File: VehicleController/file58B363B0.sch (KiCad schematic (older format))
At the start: 5 parts, among them P4 CONN_01X02, P5 MX150_8, U9 MCP2551

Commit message: Begin nailing down VC schematic details
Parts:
- added D10, D9: LED_Yel, symbol LED_Small_ALT
- added R19, R20: R_Small, symbol R_Small
- added U11: NDC7002N, symbol NDC7002N
- renumbered C11 to C12, P4 to P3, P5 to P4, R11 to R18, U9 to U12
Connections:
- net +5V: now also R19.1, R20.1
- net CANRX: now also U11.3 (G2)
- net CANTX: now also U11.1 (G1)
- net GND: now also U11.2 (S2), U11.5 (S1)
- new net: D10.1 (K), U11.4 (D2)
- new net: D9.1 (K), U11.6 (D1)
- new net: D9.2 (A), R19.2
- new net: D10.2 (A), R20.2
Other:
- moved on the sheet: C12
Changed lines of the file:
@@
 $EndDescr
 $Comp
-L MCP2551 U9
+L MCP2551 U12
 U 1 1 58B36586
 P 5450 3250
-F 0 "U9" H 5450 3737 60  0000 C CNN
+F 0 "U12" H 5450 3737 60  0000 C CNN
 F 1 "MCP2551" H 5450 3631 60  0000 C CNN
 F 2 "" H 5450 3250 60  0000 C CNN
@@
 $EndComp
 $Comp
-L GND #PWR040
+L GND #PWR46
 U 1 1 58B3658D
 P 5950 3500
-F 0 "#PWR040" H 5950 3250 50  0001 C CNN
+F 0 "#PWR46" H 5950 3250 50  0001 C CNN
 F 1 "GND" H 5955 3327 50  0000 C CNN
 F 2 "" H 5950 3500 50  0000 C CNN
@@
 NoConn ~ 5850 3050
 $Comp
-L +5V #PWR041
+L +5V #PWR44
 U 1 1 58B36594
 P 4900 2950
-F 0 "#PWR041" H 4900 2800 50  0001 C CNN
+F 0 "#PWR44" H 4900 2800 50  0001 C CNN
 F 1 "+5V" H 4915 3123 50  0000 C CNN
 F 2 "" H 4900 2950 50  0000 C CNN
@@
 $EndComp
 $Comp
-L GND #PWR042
+L GND #PWR45
 U 1 1 58B3659A
 P 4950 3550
-F 0 "#PWR042" H 4950 3300 50  0001 C CNN
+F 0 "#PWR45" H 4950 3300 50  0001 C CNN
 F 1 "GND" H 4955 3377 50  0000 C CNN
 F 2 "" H 4950 3550 50  0000 C CNN
@@
 $EndComp
 $Comp
-L R R11
+L R R18
 U 1 1 58B365A2
 P 5250 2500
-F 0 "R11" V 5043 2500 50  0000 C CNN
+F 0 "R18" V 5043 2500 50  0000 C CNN
 F 1 "120" V 5134 2500 50  0000 C CNN
 F 2 "" V 5180 2500 50  0000 C CNN
@@
 CANL
 $Comp
-L CONN_01X02 P4
+L CONN_01X02 P3
 U 1 1 58B365AA
 P 5550 2250
-F 0 "P4" V 5750 2300 50  0000 R CNN
-F 1 "CONN_01X02" V 5650 2450 50  0000 R CNN
+F 0 "P3" V 5765 2245 50  0000 C CNN
+F 1 "CONN_01X02" V 5674 2245 50  0000 C CNN
 F 2 "" H 5550 2250 50  0000 C CNN
 F 3 "" H 5550 2250 50  0000 C CNN
@@
 Text Label 5900 2500 2    60   ~ 0
 CANH
-Text HLabel 4700 3150 0    60   Input ~ 0
+Text HLabel 4800 3150 0    60   Input ~ 0
 CANTX
-Text HLabel 4700 3250 0    60   Input ~ 0
+Text HLabel 4800 3250 0    60   Input ~ 0
 CANRX
 $Comp
-L C_Small C11
+L C_Small C12
 U 1 1 58B0DDAC
-P 5250 3950
-F 0 "C11" H 5342 3996 50  0000 L CNN
-F 1 "C_Small" H 5342 3905 50  0000 L CNN
-F 2 "" H 5250 3950 50  0000 C CNN
-F 3 "" H 5250 3950 50  0000 C CNN
-	1    5250 3950
+P 4250 3200
+F 0 "C12" H 4342 3246 50  0000 L CNN
+F 1 "C_Small" H 4342 3155 50  0000 L CNN
+F 2 "" H 4250 3200 50  0000 C CNN
+F 3 "" H 4250 3200 50  0000 C CNN
+	1    4250 3200
 	-1   0    0    -1
 $EndComp
 $Comp
-L +5V #PWR043
+L +5V #PWR41
 U 1 1 58B0DEC8
-P 5250 3750
-F 0 "#PWR043" H 5250 3600 50  0001 C CNN
-F 1 "+5V" H 5265 3923 50  0000 C CNN
-F 2 "" H 5250 3750 50  0000 C CNN
-F 3 "" H 5250 3750 50  0000 C CNN
-	1    5250 3750
-	1    0    0    -1
-$EndComp
-$Comp
-L GND #PWR044
+P 4250 3000
+F 0 "#PWR41" H 4250 2850 50  0001 C CNN
+F 1 "+5V" H 4265 3173 50  0000 C CNN
+F 2 "" H 4250 3000 50  0000 C CNN
+F 3 "" H 4250 3000 50  0000 C CNN
+	1    4250 3000
+	1    0    0    -1
+$EndComp
+$Comp
+L GND #PWR42
 U 1 1 58B0DF2A
-P 5250 4200
-F 0 "#PWR044" H 5250 3950 50  0001 C CNN
-F 1 "GND" H 5255 4027 50  0000 C CNN
-F 2 "" H 5250 4200 50  0000 C CNN
-F 3 "" H 5250 4200 50  0000 C CNN
-	1    5250 4200
+P 4250 3450
+F 0 "#PWR42" H 4250 3200 50  0001 C CNN
+F 1 "GND" H 4255 3277 50  0000 C CNN
+F 2 "" H 4250 3450 50  0000 C CNN
+F 3 "" H 4250 3450 50  0000 C CNN
+	1    4250 3450
 	1    0    0    -1
 $EndComp
@@
 	4950 3350 5050 3350
 Wire Wire Line
-	5050 3150 4700 3150
-Wire Wire Line
-	4700 3250 5050 3250
+	5050 3150 4800 3150
+Wire Wire Line
+	4800 3250 5050 3250
 Wire Wire Line
 	5400 2500 5500 2500
@@
 	5600 2500 5900 2500
 Wire Wire Line
-	5250 3850 5250 3750
-Wire Wire Line
-	5250 4200 5250 4050
-$Comp
-L MX150_8 P5
+	4250 3100 4250 3000
+Wire Wire Line
+	4250 3450 4250 3300
+$Comp
+L MX150_8 P4
 U 1 1 58B7A4A8
 P 7350 3200
-F 0 "P5" H 7350 3565 50  0000 C CNN
+F 0 "P4" H 7350 3565 50  0000 C CNN
 F 1 "MX150_8" H 7350 3474 50  0000 C CNN
 F 2 "" H 7350 2000 50  0000 C CNN
@@
 	7000 3050 7100 3050
 $Comp
-L GND #PWR045
+L GND #PWR49
 U 1 1 58B7F609
 P 7000 3450
-F 0 "#PWR045" H 7000 3200 50  0001 C CNN
+F 0 "#PWR49" H 7000 3200 50  0001 C CNN
 F 1 "GND" H 7005 3277 50  0000 C CNN
 F 2 "" H 7000 3450 50  0000 C CNN
@@
 	7700 3050 7700 2950
 $Comp
-L GND #PWR046
+L GND #PWR51
 U 1 1 58B7FA08
 P 7700 3450
-F 0 "#PWR046" H 7700 3200 50  0001 C CNN
+F 0 "#PWR51" H 7700 3200 50  0001 C CNN
 F 1 "GND" H 7705 3277 50  0000 C CNN
 F 2 "" H 7700 3450 50  0000 C CNN
@@
 	7700 3350 7700 3450
 $Comp
-L +12V #PWR047
+L +12V #PWR48
 U 1 1 58BABA64
 P 7000 2950
-F 0 "#PWR047" H 7000 2800 50  0001 C CNN
+F 0 "#PWR48" H 7000 2800 50  0001 C CNN
 F 1 "+12V" H 7015 3123 50  0000 C CNN
 F 2 "" H 7000 2950 50  0000 C CNN
@@
 $EndComp
 $Comp
-L +12V #PWR048
+L +12V #PWR50
 U 1 1 58BABA85
 P 7700 2950
-F 0 "#PWR048" H 7700 2800 50  0001 C CNN
+F 0 "#PWR50" H 7700 2800 50  0001 C CNN
 F 1 "+12V" H 7715 3123 50  0000 C CNN
 F 2 "" H 7700 2950 50  0000 C CNN
@@
 	1    0    0    -1
 $EndComp
+$Comp
+L NDC7002N U11
+U 1 1 58C2C3D8
+P 5150 4750
+F 0 "U11" H 5150 5147 60  0000 C CNN
+F 1 "NDC7002N" H 5150 5041 60  0000 C CNN
+F 2 "" H 1200 1900 60  0000 C CNN
+F 3 "" H 1200 1900 60  0000 C CNN
+	1    5150 4750
+	1    0    0    -1
+$EndComp
+Text HLabel 4600 4600 0    60   Input ~ 0
+CANTX
+Text HLabel 4600 4700 0    60   Input ~ 0
+CANRX
+Wire Wire Line
+	4600 4600 4800 4600
+Wire Wire Line
+	4600 4700 4800 4700
+$Comp
+L GND #PWR43
+U 1 1 58C2C777
+P 4700 5000
+F 0 "#PWR43" H 1200 2500 50  0001 C CNN
+F 1 "GND" H 4705 4827 50  0000 C CNN
+F 2 "" H 1200 2750 50  0001 C CNN
+F 3 "" H 1200 2750 50  0001 C CNN
+	1    4700 5000
+	1    0    0    -1
+$EndComp
+Wire Wire Line
+	4700 4800 4700 5000
+Wire Wire Line
+	4700 4800 4800 4800
+Wire Wire Line
+	4800 4900 4700 4900
+Connection ~ 4700 4900
+$Comp
+L LED_Small_ALT D9
+U 1 1 58C2C900
+P 5650 4650
+F 0 "D9" H 5650 4885 50  0000 C CNN
+F 1 "LED_Yel" H 5650 4794 50  0000 C CNN
+F 2 "" V 1100 3550 50  0001 C CNN
+F 3 "" V 1100 3550 50  0001 C CNN
+	1    5650 4650
+	1    0    0    -1
+$EndComp
+$Comp
+L LED_Small_ALT D10
+U 1 1 58C2C94C
+P 5650 4850
+F 0 "D10" H 5550 4750 50  0000 C CNN
+F 1 "LED_Yel" H 5550 4650 50  0000 C CNN
+F 2 "" V 1100 3750 50  0001 C CNN
+F 3 "" V 1100 3750 50  0001 C CNN
+	1    5650 4850
+	1    0    0    -1
+$EndComp
+Wire Wire Line
+	5550 4650 5500 4650
+Wire Wire Line
+	5500 4850 5550 4850
+$Comp
+L R_Small R19
+U 1 1 58C2D567
+P 5950 4650
+F 0 "R19" V 5750 4750 50  0000 C CNN
+F 1 "R_Small" V 5850 4750 50  0000 C CNN
+F 2 "" H 550 3100 50  0001 C CNN
+F 3 "" H 550 3100 50  0001 C CNN
+	1    5950 4650
+	0    1    1    0
+$EndComp
+$Comp
+L R_Small R20
+U 1 1 58C2D5C7
+P 5950 4850
+F 0 "R20" V 6054 4850 50  0000 C CNN
+F 1 "R_Small" V 6145 4850 50  0000 C CNN
+F 2 "" H 550 3300 50  0001 C CNN
+F 3 "" H 550 3300 50  0001 C CNN
+	1    5950 4850
+	0    1    1    0
+$EndComp
+Wire Wire Line
+	5850 4650 5750 4650
+Wire Wire Line
+	5750 4850 5850 4850
+$Comp
+L +5V #PWR47
+U 1 1 58C2D6D1
+P 6350 4450
+F 0 "#PWR47" H 850 2600 50  0001 C CNN
+F 1 "+5V" H 6365 4623 50  0000 C CNN
+F 2 "" H 850 2750 50  0001 C CNN
+F 3 "" H 850 2750 50  0001 C CNN
+	1    6350 4450
+	1    0    0    -1
+$EndComp
+Wire Wire Line
+	6050 4650 6350 4650
+Wire Wire Line
+	6350 4450 6350 4850
+Wire Wire Line
+	6350 4850 6050 4850
+Connection ~ 6350 4650
 $EndSCHEMATC

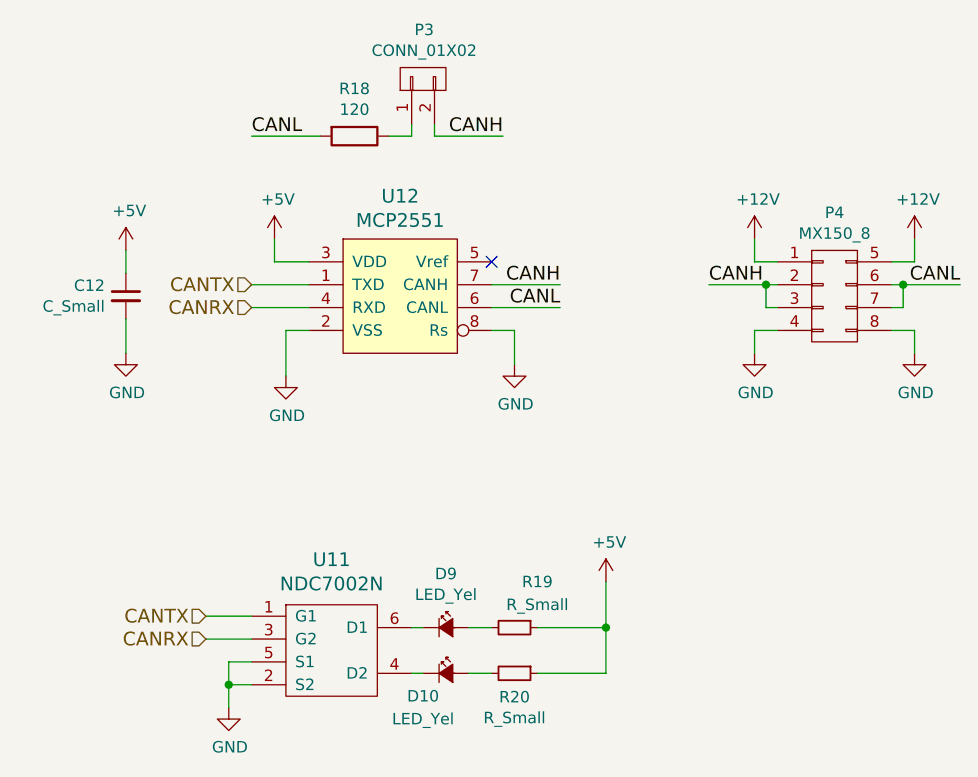
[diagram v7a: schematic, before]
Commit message: Finish VCU schematic, most footprint selections.  Start layout
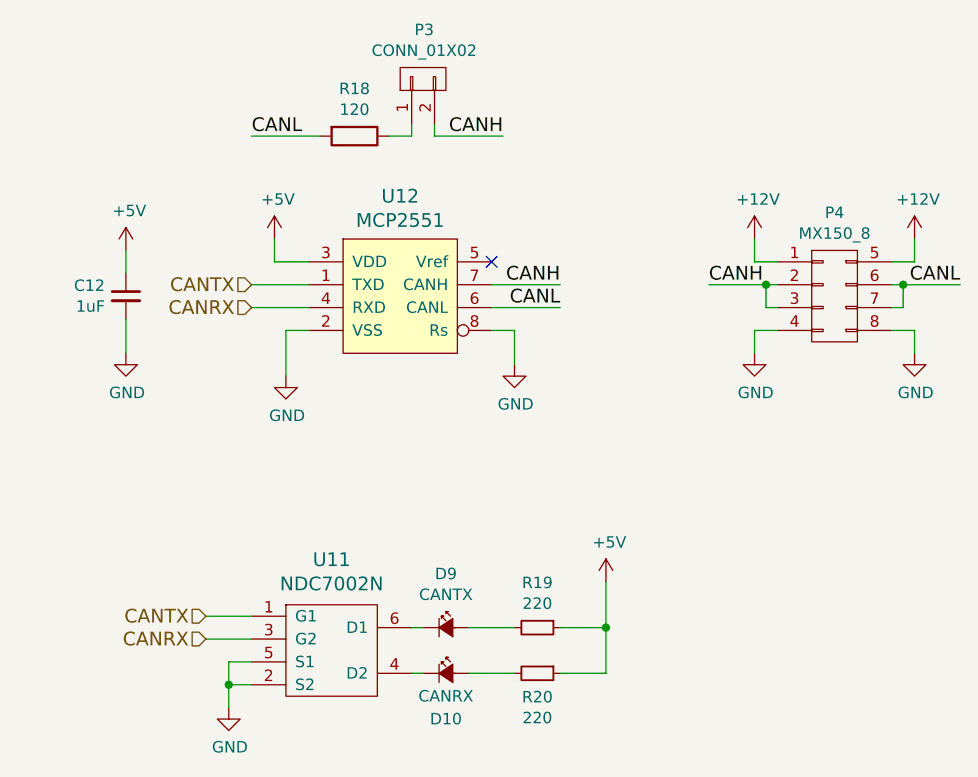
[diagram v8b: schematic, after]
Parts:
- C12: value C_Small -> 1uF; footprint (none) -> Capacitors_SMD:C_0805_HandSoldering
- D10: value LED_Yel -> CANRX; footprint (none) -> LEDs:LED-0805
- D9: value LED_Yel -> CANTX; footprint (none) -> LEDs:LED-0805
- P3: footprint (none) -> Pin_Headers:Pin_Header_Angled_1x02
- P4: footprint (none) -> UNCAMotorsports:MX150_8Pin
- R18: footprint (none) -> Resistors_SMD:R_0805_HandSoldering
- R19, R20: value R_Small -> 220; footprint (none) -> Resistors_SMD:R_0805_HandSoldering
- U11: footprint (none) -> TO_SOT_Packages_SMD:SOT-23-6
- U12: footprint (none) -> SMD_Packages:SOIC-8-N
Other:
- moved on the sheet: R19, R20
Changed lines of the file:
@@
 encoding utf-8
 Sheet 4 5
-Title ""
-Date ""
-Rev ""
-Comp ""
+Title "Vehicle Controller"
+Date "2017-03-11"
+Rev "001"
+Comp "UNC Asheville Motorsports"
 Comment1 ""
 Comment2 ""
@@
 F 0 "U12" H 5450 3737 60  0000 C CNN
 F 1 "MCP2551" H 5450 3631 60  0000 C CNN
-F 2 "" H 5450 3250 60  0000 C CNN
+F 2 "SMD_Packages:SOIC-8-N" H 5450 3250 60  0001 C CNN
 F 3 "" H 5450 3250 60  0000 C CNN
 	1    5450 3250
@@
 $EndComp
 $Comp
-L GND #PWR46
+L GND #PWR044
 U 1 1 58B3658D
 P 5950 3500
-F 0 "#PWR46" H 5950 3250 50  0001 C CNN
+F 0 "#PWR044" H 5950 3250 50  0001 C CNN
 F 1 "GND" H 5955 3327 50  0000 C CNN
 F 2 "" H 5950 3500 50  0000 C CNN
@@
 NoConn ~ 5850 3050
 $Comp
-L +5V #PWR44
+L +5V #PWR045
 U 1 1 58B36594
 P 4900 2950
-F 0 "#PWR44" H 4900 2800 50  0001 C CNN
+F 0 "#PWR045" H 4900 2800 50  0001 C CNN
 F 1 "+5V" H 4915 3123 50  0000 C CNN
 F 2 "" H 4900 2950 50  0000 C CNN
@@
 $EndComp
 $Comp
-L GND #PWR45
+L GND #PWR046
 U 1 1 58B3659A
 P 4950 3550
-F 0 "#PWR45" H 4950 3300 50  0001 C CNN
+F 0 "#PWR046" H 4950 3300 50  0001 C CNN
 F 1 "GND" H 4955 3377 50  0000 C CNN
 F 2 "" H 4950 3550 50  0000 C CNN
@@
 F 0 "R18" V 5043 2500 50  0000 C CNN
 F 1 "120" V 5134 2500 50  0000 C CNN
-F 2 "" V 5180 2500 50  0000 C CNN
+F 2 "Resistors_SMD:R_0805_HandSoldering" V 5180 2500 50  0001 C CNN
 F 3 "" H 5250 2500 50  0000 C CNN
 	1    5250 2500
@@
 F 0 "P3" V 5765 2245 50  0000 C CNN
 F 1 "CONN_01X02" V 5674 2245 50  0000 C CNN
-F 2 "" H 5550 2250 50  0000 C CNN
+F 2 "Pin_Headers:Pin_Header_Angled_1x02" H 5550 2250 50  0001 C CNN
 F 3 "" H 5550 2250 50  0000 C CNN
 	1    5550 2250
@@
 P 4250 3200
 F 0 "C12" H 4342 3246 50  0000 L CNN
-F 1 "C_Small" H 4342 3155 50  0000 L CNN
-F 2 "" H 4250 3200 50  0000 C CNN
+F 1 "1uF" H 4342 3155 50  0000 L CNN
+F 2 "Capacitors_SMD:C_0805_HandSoldering" H 4250 3200 50  0001 C CNN
 F 3 "" H 4250 3200 50  0000 C CNN
 	1    4250 3200
@@
 $EndComp
 $Comp
-L +5V #PWR41
+L +5V #PWR047
 U 1 1 58B0DEC8
 P 4250 3000
-F 0 "#PWR41" H 4250 2850 50  0001 C CNN
+F 0 "#PWR047" H 4250 2850 50  0001 C CNN
 F 1 "+5V" H 4265 3173 50  0000 C CNN
 F 2 "" H 4250 3000 50  0000 C CNN
@@
 $EndComp
 $Comp
-L GND #PWR42
+L GND #PWR048
 U 1 1 58B0DF2A
 P 4250 3450
-F 0 "#PWR42" H 4250 3200 50  0001 C CNN
+F 0 "#PWR048" H 4250 3200 50  0001 C CNN
 F 1 "GND" H 4255 3277 50  0000 C CNN
 F 2 "" H 4250 3450 50  0000 C CNN
@@
 F 0 "P4" H 7350 3565 50  0000 C CNN
 F 1 "MX150_8" H 7350 3474 50  0000 C CNN
-F 2 "" H 7350 2000 50  0000 C CNN
+F 2 "UNCAMotorsports:MX150_8Pin" H 7350 2000 50  0001 C CNN
 F 3 "" H 7350 2000 50  0000 C CNN
 	1    7350 3200
@@
 	7000 3050 7100 3050
 $Comp
-L GND #PWR49
+L GND #PWR049
 U 1 1 58B7F609
 P 7000 3450
-F 0 "#PWR49" H 7000 3200 50  0001 C CNN
+F 0 "#PWR049" H 7000 3200 50  0001 C CNN
 F 1 "GND" H 7005 3277 50  0000 C CNN
 F 2 "" H 7000 3450 50  0000 C CNN
@@
 	7700 3050 7700 2950
 $Comp
-L GND #PWR51
+L GND #PWR050
 U 1 1 58B7FA08
 P 7700 3450
-F 0 "#PWR51" H 7700 3200 50  0001 C CNN
+F 0 "#PWR050" H 7700 3200 50  0001 C CNN
 F 1 "GND" H 7705 3277 50  0000 C CNN
 F 2 "" H 7700 3450 50  0000 C CNN
@@
 	7700 3350 7700 3450
 $Comp
-L +12V #PWR48
+L +12V #PWR051
 U 1 1 58BABA64
 P 7000 2950
-F 0 "#PWR48" H 7000 2800 50  0001 C CNN
+F 0 "#PWR051" H 7000 2800 50  0001 C CNN
 F 1 "+12V" H 7015 3123 50  0000 C CNN
 F 2 "" H 7000 2950 50  0000 C CNN
@@
 $EndComp
 $Comp
-L +12V #PWR50
+L +12V #PWR052
 U 1 1 58BABA85
 P 7700 2950
-F 0 "#PWR50" H 7700 2800 50  0001 C CNN
+F 0 "#PWR052" H 7700 2800 50  0001 C CNN
 F 1 "+12V" H 7715 3123 50  0000 C CNN
 F 2 "" H 7700 2950 50  0000 C CNN
@@
 F 0 "U11" H 5150 5147 60  0000 C CNN
 F 1 "NDC7002N" H 5150 5041 60  0000 C CNN
-F 2 "" H 1200 1900 60  0000 C CNN
+F 2 "TO_SOT_Packages_SMD:SOT-23-6" H 1200 1900 60  0001 C CNN
 F 3 "" H 1200 1900 60  0000 C CNN
 	1    5150 4750
@@
 	4600 4700 4800 4700
 $Comp
-L GND #PWR43
+L GND #PWR053
 U 1 1 58C2C777
 P 4700 5000
-F 0 "#PWR43" H 1200 2500 50  0001 C CNN
+F 0 "#PWR053" H 1200 2500 50  0001 C CNN
 F 1 "GND" H 4705 4827 50  0000 C CNN
 F 2 "" H 1200 2750 50  0001 C CNN
@@
 P 5650 4650
 F 0 "D9" H 5650 4885 50  0000 C CNN
-F 1 "LED_Yel" H 5650 4794 50  0000 C CNN
-F 2 "" V 1100 3550 50  0001 C CNN
+F 1 "CANTX" H 5650 4794 50  0000 C CNN
+F 2 "LEDs:LED-0805" V 1100 3550 50  0001 C CNN
 F 3 "" V 1100 3550 50  0001 C CNN
 	1    5650 4650
@@
 U 1 1 58C2C94C
 P 5650 4850
-F 0 "D10" H 5550 4750 50  0000 C CNN
-F 1 "LED_Yel" H 5550 4650 50  0000 C CNN
-F 2 "" V 1100 3750 50  0001 C CNN
+F 0 "D10" H 5650 4650 50  0000 C CNN
+F 1 "CANRX" H 5650 4750 50  0000 C CNN
+F 2 "LEDs:LED-0805" V 1100 3750 50  0001 C CNN
 F 3 "" V 1100 3750 50  0001 C CNN
 	1    5650 4850
@@
 L R_Small R19
 U 1 1 58C2D567
-P 5950 4650
-F 0 "R19" V 5750 4750 50  0000 C CNN
-F 1 "R_Small" V 5850 4750 50  0000 C CNN
-F 2 "" H 550 3100 50  0001 C CNN
-F 3 "" H 550 3100 50  0001 C CNN
-	1    5950 4650
+P 6050 4650
+F 0 "R19" V 5854 4650 50  0000 C CNN
+F 1 "220" V 5945 4650 50  0000 C CNN
+F 2 "Resistors_SMD:R_0805_HandSoldering" H 650 3100 50  0001 C CNN
+F 3 "" H 650 3100 50  0001 C CNN
+	1    6050 4650
 	0    1    1    0
 $EndComp
@@
 L R_Small R20
 U 1 1 58C2D5C7
-P 5950 4850
-F 0 "R20" V 6054 4850 50  0000 C CNN
-F 1 "R_Small" V 6145 4850 50  0000 C CNN
-F 2 "" H 550 3300 50  0001 C CNN
-F 3 "" H 550 3300 50  0001 C CNN
-	1    5950 4850
+P 6050 4850
+F 0 "R20" V 6154 4850 50  0000 C CNN
+F 1 "220" V 6245 4850 50  0000 C CNN
+F 2 "Resistors_SMD:R_0805_HandSoldering" H 650 3300 50  0001 C CNN
+F 3 "" H 650 3300 50  0001 C CNN
+	1    6050 4850
 	0    1    1    0
 $EndComp
 Wire Wire Line
-	5850 4650 5750 4650
-Wire Wire Line
-	5750 4850 5850 4850
-$Comp
-L +5V #PWR47
+	5950 4650 5750 4650
+Wire Wire Line
+	5750 4850 5950 4850
+$Comp
+L +5V #PWR054
 U 1 1 58C2D6D1
 P 6350 4450
-F 0 "#PWR47" H 850 2600 50  0001 C CNN
+F 0 "#PWR054" H 850 2600 50  0001 C CNN
 F 1 "+5V" H 6365 4623 50  0000 C CNN
 F 2 "" H 850 2750 50  0001 C CNN
@@
 $EndComp
 Wire Wire Line
-	6050 4650 6350 4650
+	6150 4650 6350 4650
 Wire Wire Line
 	6350 4450 6350 4850
 Wire Wire Line
-	6350 4850 6050 4850
+	6350 4850 6150 4850
 Connection ~ 6350 4650
 $EndSCHEMATC
